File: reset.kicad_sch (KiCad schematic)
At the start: 13 parts, among them Q1 2N7002, Q2 2N7002

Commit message: add level shifter for rgb data line
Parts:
- C5: footprint Capacitor_Tantalum_SMD:CP_EIA-3216-18_Kemet-A -> Capacitor_SMD:C_1206_3216Metric
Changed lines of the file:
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@@
       (effects (font (size 1.27 1.27)) (justify left))
     )
-    (property "Footprint" "Capacitor_Tantalum_SMD:CP_EIA-3216-18_Kemet-A" (at 68.58 31.115 0)
+    (property "Footprint" "Capacitor_SMD:C_1206_3216Metric" (at 68.58 31.115 0)
       (effects (font (size 1.27 1.27)) hide)
     )

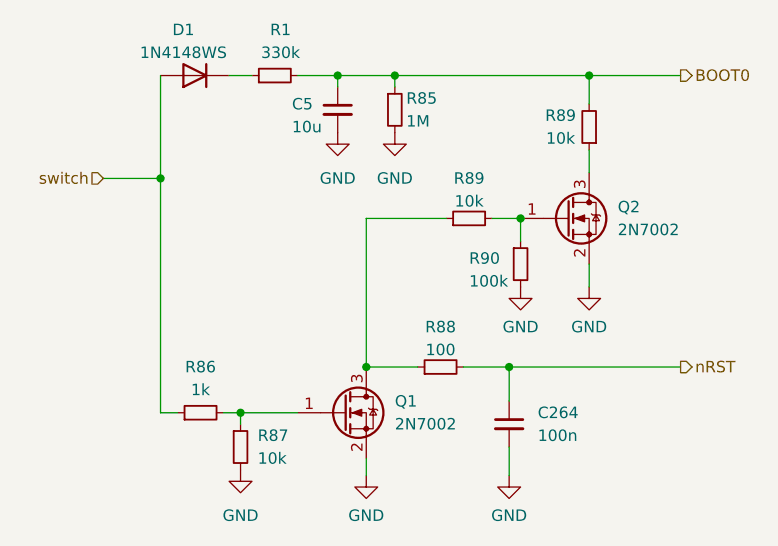
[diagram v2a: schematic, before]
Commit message: add reverse polarity protection to LDO
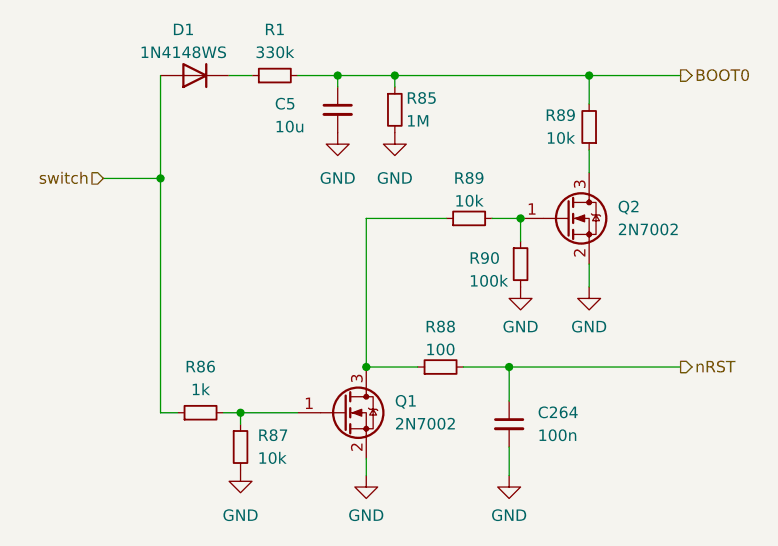
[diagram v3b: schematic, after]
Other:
- title: (none) -> MoonBoard
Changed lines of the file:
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@@
 (kicad_sch (version 20230121) (generator eeschema)
   (paper "A4")
+  (title_block
+    (title "MoonBoard")
+  )
   (junction (at 57.785 64.77) (diameter 0) (color 0 0 0 0)
   )
@@
   (symbol (lib_id "Device:C_Small") (at 68.58 31.115 0) (unit 1)
     (in_bom yes) (on_board yes) (dnp no)
-    (property "Reference" "C5" (at 63.5 30.48 0)
-      (effects (font (size 1.27 1.27)) (justify left))
-    )
-    (property "Value" "10u" (at 63.5 33.02 0)
+    (property "Reference" "C5" (at 61.595 30.48 0)
+      (effects (font (size 1.27 1.27)) (justify left))
+    )
+    (property "Value" "10u" (at 61.595 33.02 0)
       (effects (font (size 1.27 1.27)) (justify left))
     )
@@
   (symbol (lib_id "Device:R_Small") (at 61.595 27.305 90) (unit 1)
     (in_bom yes) (on_board yes) (dnp no)
-    (property "Reference" "R1" (at 62.23 22.225 90)
-      (effects (font (size 1.27 1.27)))
-    )
-    (property "Value" "330k" (at 62.23 24.765 90)
-      (effects (font (size 1.27 1.27)))
-    )
+    (property "Reference" "R1" (at 61.595 22.225 90)
+      (effects (font (size 1.27 1.27)))
+    )
+    (property "Value" "330k" (at 61.595 24.765 90)
+      (effects (font (size 1.27 1.27)))
+    )

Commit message: buzz
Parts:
- R1: footprint Resistor_SMD:R_0402_1005Metric -> Resistor_SMD:R_0603_1608Metric
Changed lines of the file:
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@@
       (effects (font (size 1.27 1.27)))
     )
-    (property "Footprint" "Resistor_SMD:R_0402_1005Metric" (at 61.595 27.305 0)
+    (property "Footprint" "Resistor_SMD:R_0603_1608Metric" (at 61.595 27.305 0)
       (effects (font (size 1.27 1.27)) hide)
     )

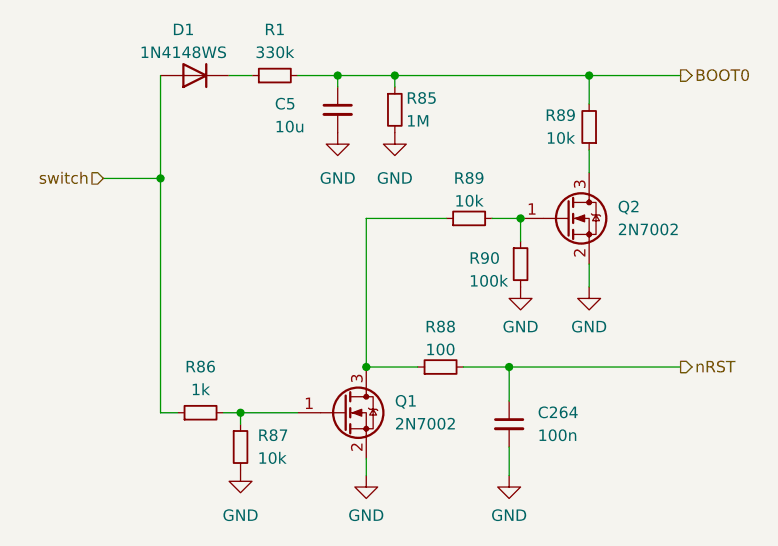
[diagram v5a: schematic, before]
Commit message: add 0R usb termination resistors change muxes to 3V3
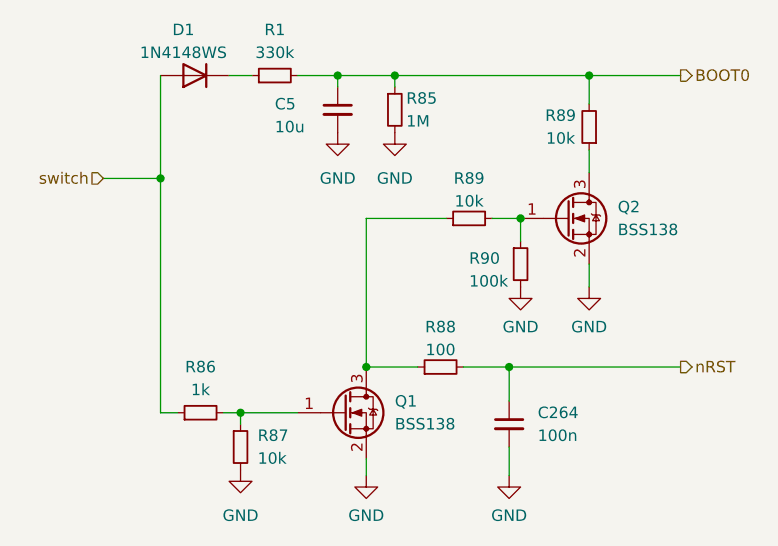
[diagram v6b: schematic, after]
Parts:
- Q1, Q2: value 2N7002 -> BSS138
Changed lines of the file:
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@@
       (effects (font (size 1.27 1.27)) (justify left))
     )
-    (property "Value" "2N7002" (at 74.93 66.04 0)
+    (property "Value" "BSS138" (at 74.93 66.04 0)
       (effects (font (size 1.27 1.27)) (justify left))
     )
@@
   )
   (symbol (lib_id "Transistor_FET:2N7002") (at 93.98 43.18 0) (unit 1)
-    (in_bom yes) (on_board yes) (dnp no) (fields_autoplaced)
+    (in_bom yes) (on_board yes) (dnp no)
     (property "Reference" "Q2" (at 99.695 41.91 0)
       (effects (font (size 1.27 1.27)) (justify left))
     )
-    (property "Value" "2N7002" (at 99.695 44.45 0)
+    (property "Value" "BSS138" (at 99.695 44.45 0)
       (effects (font (size 1.27 1.27)) (justify left))
     )

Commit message: update to kicad 8
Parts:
- renumbered C5 to C183, C264 to C184, Q2 to Q1, Q1 to Q2, R1 to R91, R85 to R92, R89 to R93, R89 to R94, R90 to R95, R88 to R96, R86 to R97, R87 to R98
